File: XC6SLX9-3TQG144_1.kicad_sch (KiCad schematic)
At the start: 11 parts, among them U1 XC6SLX9-3TQG144, U2 SST25VF040B-50-4C-SAF-T

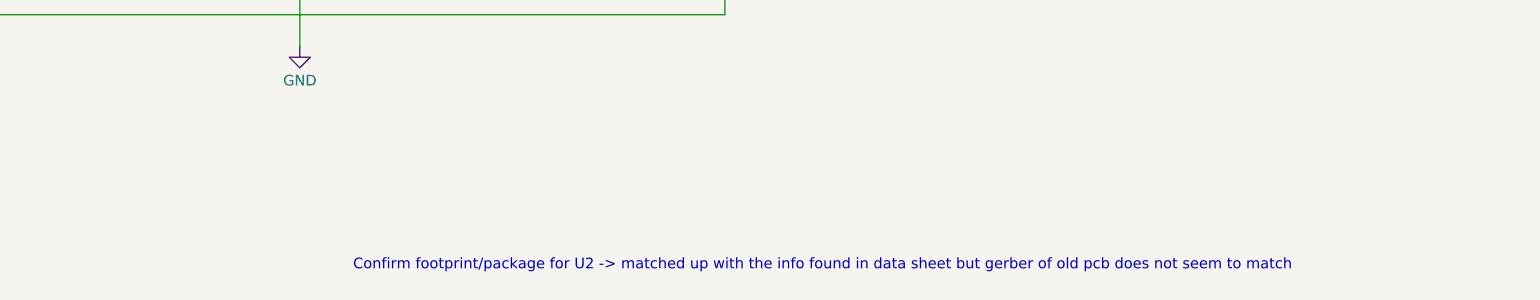
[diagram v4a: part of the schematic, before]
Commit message: updated note on schematic
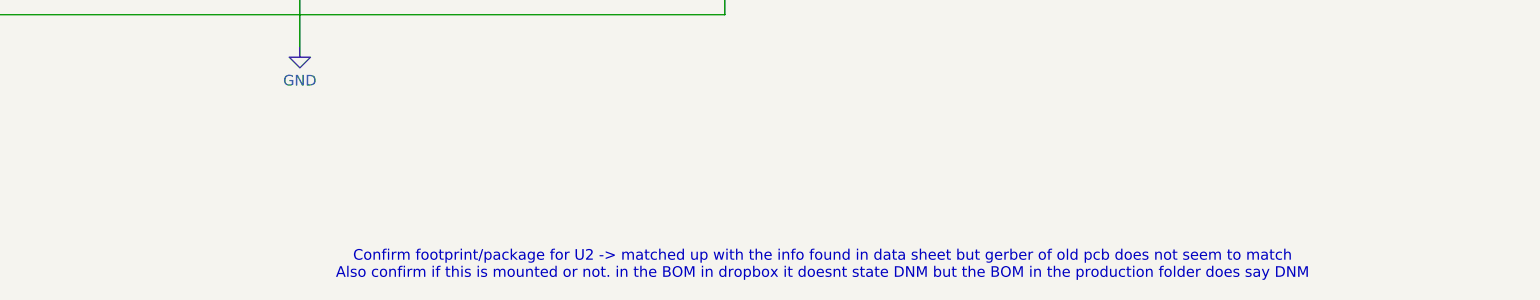
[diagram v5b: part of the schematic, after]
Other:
- note added: "Confirm footprint/package for U2 -> matched up with the info found in data sheet but gerber of old pcb does not seem to match Also confirm if this is mounted or not. in the BOM in dropbox it doesnt state DNM but the BOM in the production folder does say DNM"
- note removed: "Confirm footprint/package for U2 -> matched up with the info found in data sheet but gerber of old pcb does not seem to match"
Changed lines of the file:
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@@
 		)
 	)
-	(text "Confirm footprint/package for U2 -> matched up with the info found in data sheet but gerber of old pcb does not seem to match"
+	(text "Confirm footprint/package for U2 -> matched up with the info found in data sheet but gerber of old pcb does not seem to match\nAlso confirm if this is mounted or not. in the BOM in dropbox it doesnt state DNM but the BOM in the production folder does say DNM"
 		(exclude_from_sim no)
 		(at 174.244 215.392 0)

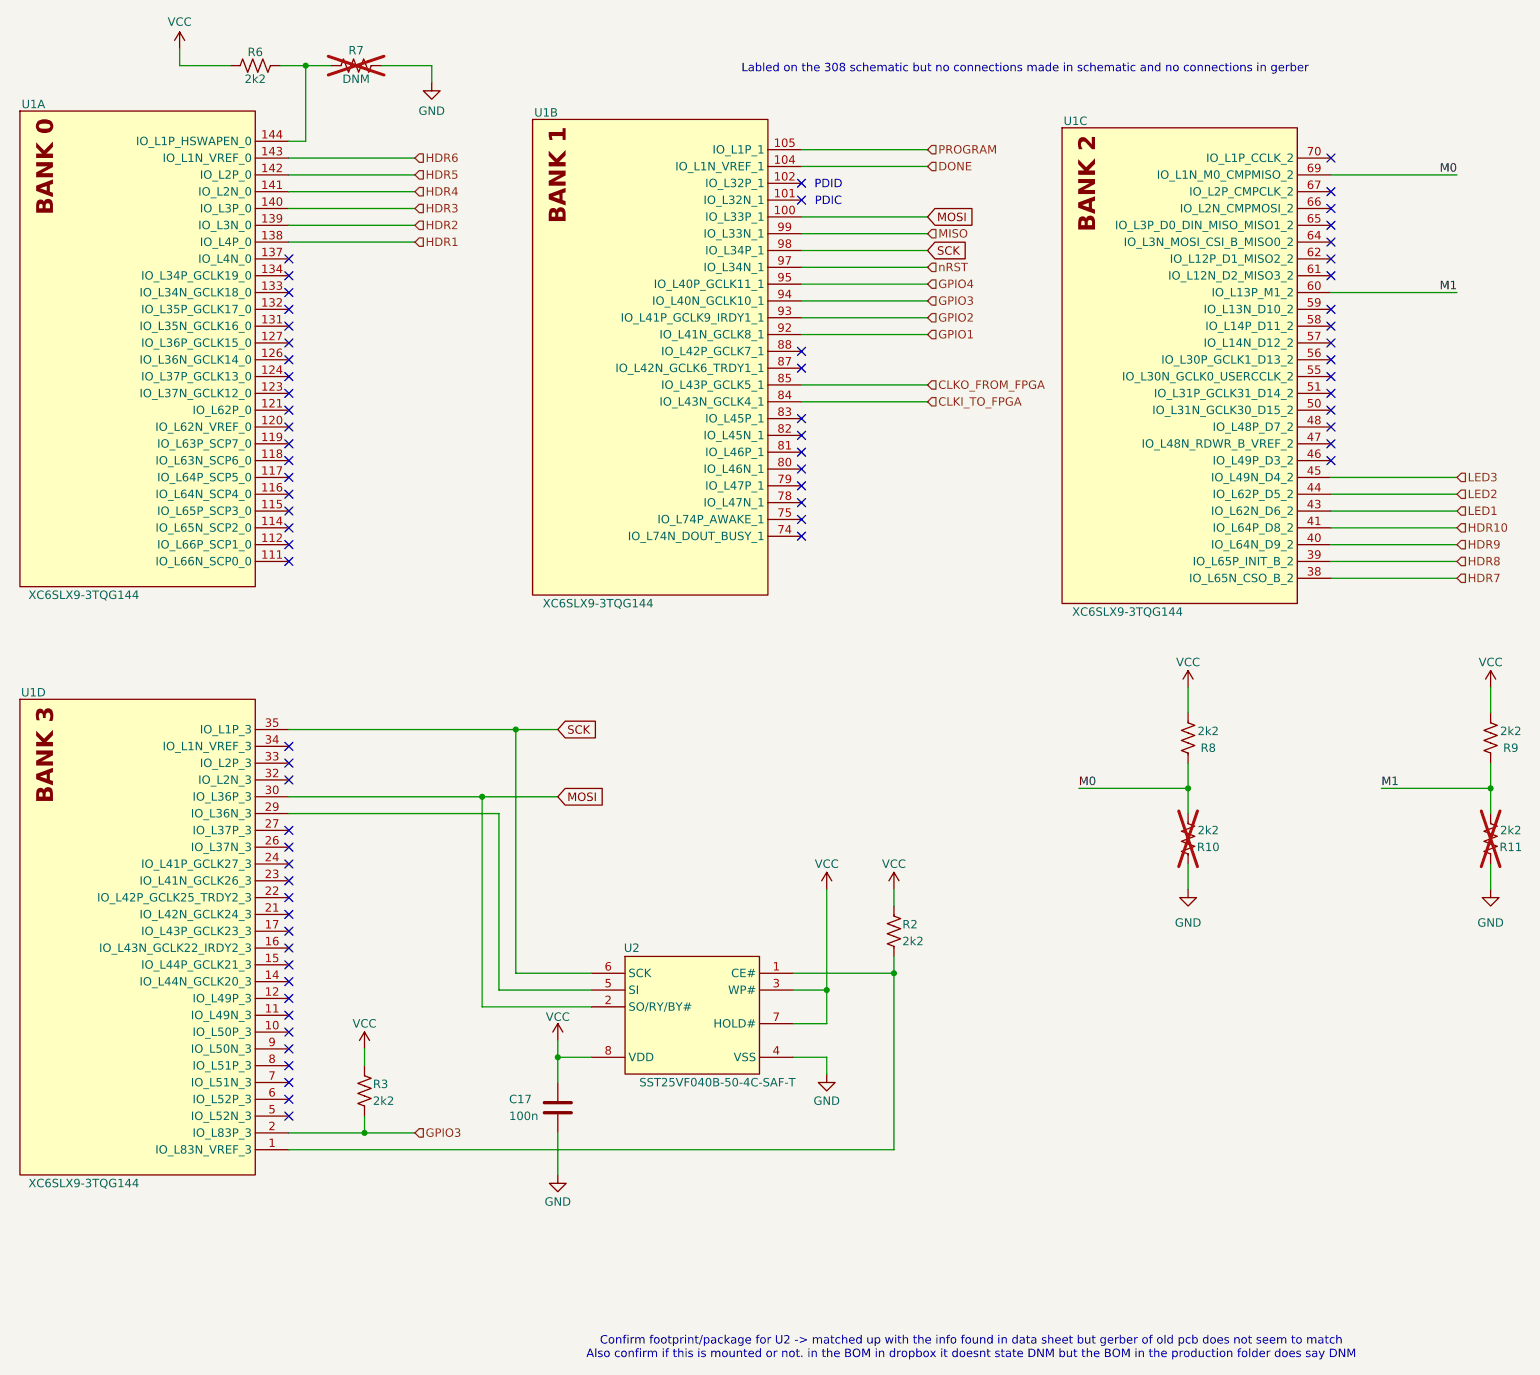
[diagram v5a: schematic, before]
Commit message: updated schematic and pcb after library re-organization
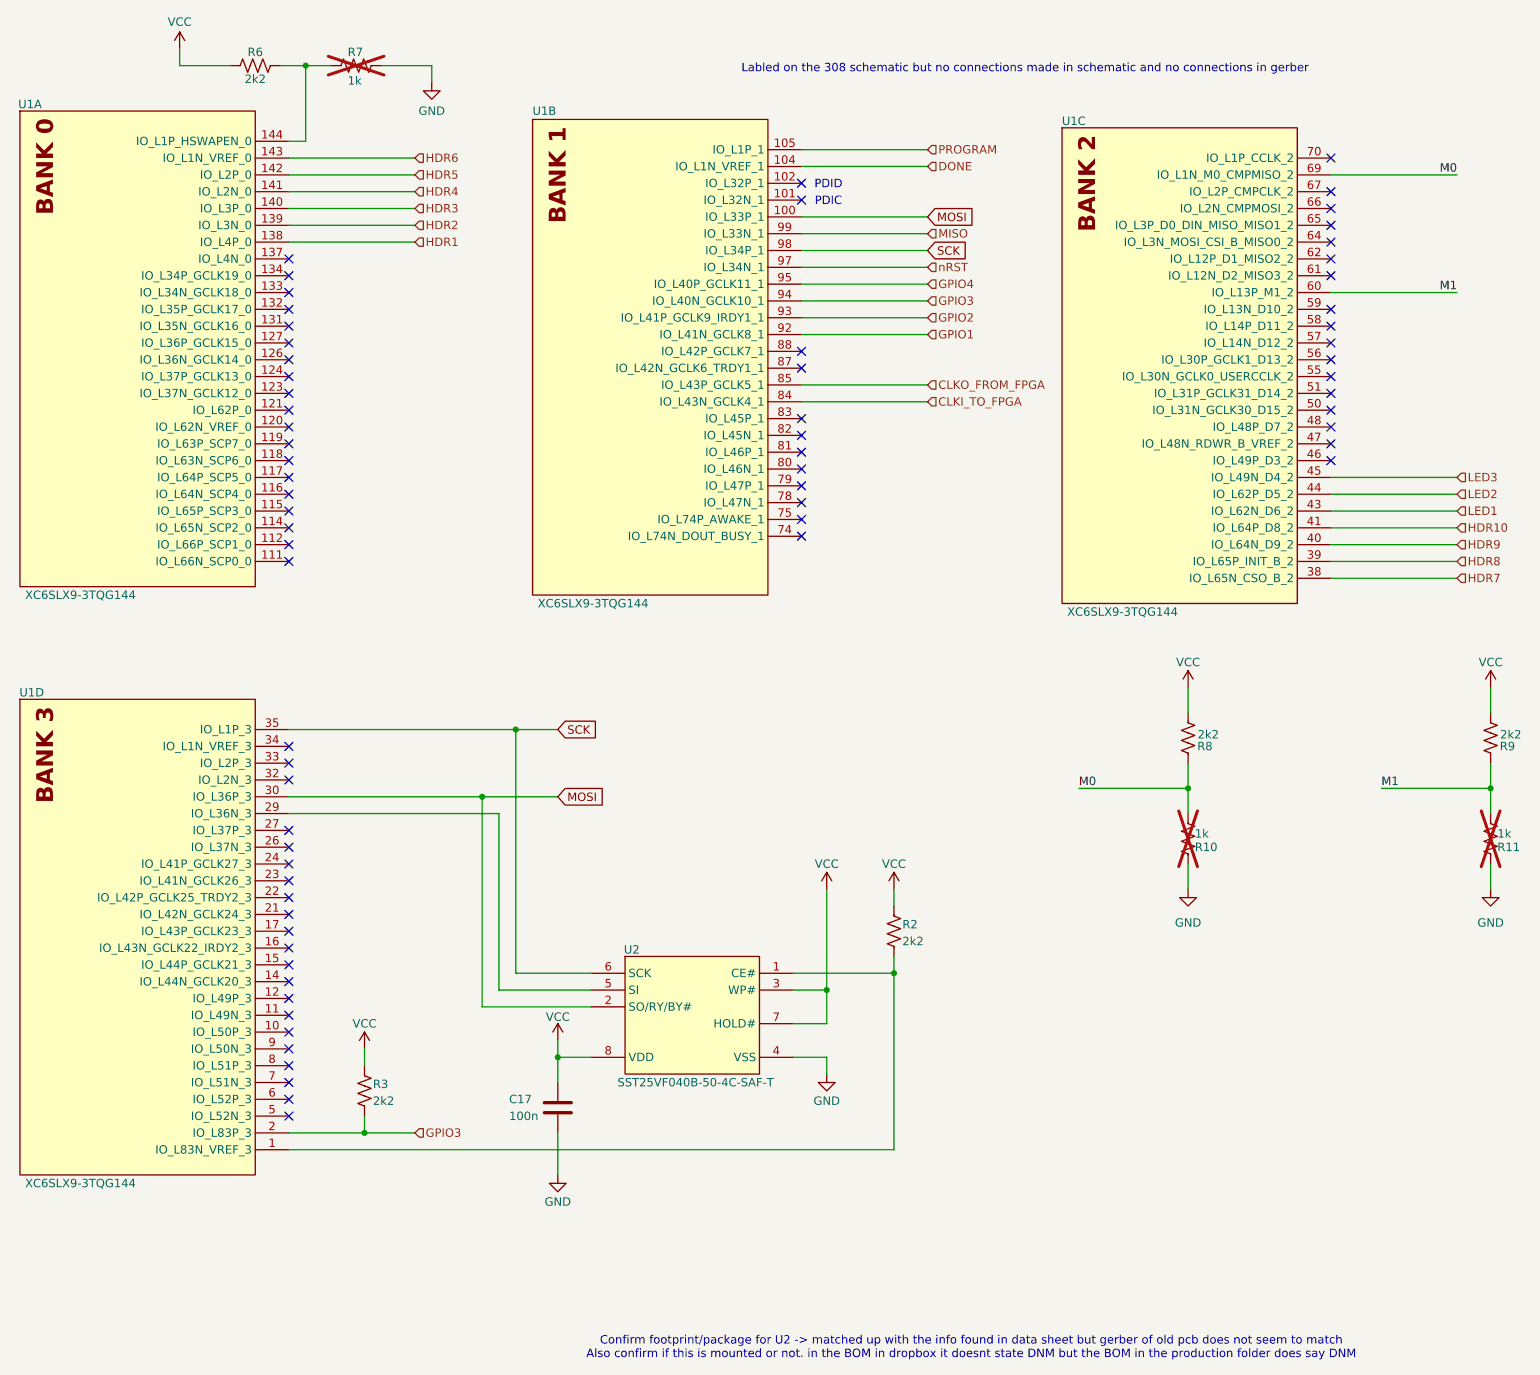
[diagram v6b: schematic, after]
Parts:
- removed R10, R11: RES_2k2_0603, Resistor_SMD:R_0603_1608Metric, symbol 0603_Yageo_Res:RES_2k2_0603
- removed R7: DNM_0603, Resistor_SMD:R_0603_1608Metric, symbol tutorial_2_library:DNM_RES_0603_1
- removed U1: XC6SLX9-3TQG144, Package_QFP:TQFP-144_20x20mm_P0.5mm, symbol tutorial_2_library:XC6SLX9-3TQG144
- removed U2: SST25VF040B-50-4C-SAF-T, Package_SO:SOIC-8_5.275x5.275mm_P1.27mm, symbol tutorial_2_library:SST25VF040B-50-4C-SAF-T
- added R10, R11, R7: RES_1k_0603, Resistor_SMD:R_0603_1608Metric, symbol 0603_Yageo_Res:RES_1k_0603
- added U1: XC6SLX9-3TQG144, Package_QFP:TQFP-144_20x20mm_P0.5mm, symbol Integrated_Circuits:XC6SLX9-3TQG144
- added U2: SST25VF040B-50-4C-SAF-T, Package_SO:SOIC-8_5.275x5.275mm_P1.27mm, symbol Integrated_Circuits:SST25VF040B-50-4C-SAF-T
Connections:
- net CLKI_TO_FPGA: now also U1.84 (IO_L43N_GCLK4_1)
- net CLKO_FROM_FPGA: now also U1.85 (IO_L43P_GCLK5_1)
- net DONE: now also U1.104 (IO_L1N_VREF_1)
- net GND: now also R10.1, R11.1, R7.1, U2.4 (VSS)
- net GPIO1: now also U1.92 (IO_L41N_GCLK8_1)
- net GPIO2: now also U1.93 (IO_L41P_GCLK9_IRDY1_1)
- net GPIO3: now also U1.2 (IO_L83P_3), U1.94 (IO_L40N_GCLK10_1)
- net GPIO4: now also U1.95 (IO_L40P_GCLK11_1)
- net HDR1: now also U1.138 (IO_L4P_0)
- net HDR10: now also U1.41 (IO_L64P_D8_2)
- net HDR2: now also U1.139 (IO_L3N_0)
- net HDR3: now also U1.140 (IO_L3P_0)
- net HDR4: now also U1.141 (IO_L2N_0)
- net HDR5: now also U1.142 (IO_L2P_0)
- net HDR6: now also U1.143 (IO_L1N_VREF_0)
- net HDR7: now also U1.38 (IO_L65N_CSO_B_2)
- net HDR8: now also U1.39 (IO_L65P_INIT_B_2)
- net HDR9: now also U1.40 (IO_L64N_D9_2)
- net LED1: now also U1.43 (IO_L62N_D6_2)
- net LED2: now also U1.44 (IO_L62P_D5_2)
- net LED3: now also U1.45 (IO_L49N_D4_2)
- net M0: now also R10.2, U1.69 (IO_L1N_M0_CMPMISO_2)
- net M1: now also R11.2, U1.60 (IO_L13P_M1_2)
- net MISO: now also U1.99 (IO_L33N_1)
- net MOSI: now also U1.100 (IO_L33P_1), U1.30 (IO_L36P_3), U2.2 (SO/RY/BY#)
- net PROGRAM: now also U1.105 (IO_L1P_1)
- net SCK: now also U1.35 (IO_L1P_3), U1.98 (IO_L34P_1), U2.6 (SCK)
- net VCC: now also U2.3 (WP#), U2.7 (HOLD#), U2.8 (VDD)
- net nRST: now also U1.97 (IO_L34N_1)
- net at R6.2: now also R7.2, U1.144 (IO_L1P_HSWAPEN_0)
- net at R2.1: now also U1.1 (IO_L83N_VREF_3), U2.1 (CE#)
- new net: U1.29 (IO_L36N_3), U2.5 (SI)
